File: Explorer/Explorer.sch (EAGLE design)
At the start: 42 parts, among them J4 POWER_JACK

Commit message: updated explorer board
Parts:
- removed D10, D11, D12, D13, D3, D4, D5, D6, D7, D8, D9: (no value), SparkFun-LED:LED0603
- removed D2: 1N4001, SparkFun-DiscreteSemi:DIODE-KIT2
- removed R2: 10k, SparkFun-Resistors:10KOHM-0603-1/10W-1%
- removed RESET: SKRKAEE020, D3ltav's Custom:SMD-BUTTON(2P-3.9X2.9X1.5+0.4MM)-SKRKAEE020
- added P10, P11, P12, P13, P2, P3, P4, P5, P6, P7, P8, P9: (no value), SparkFun-LED:LED0603
- added Q1, Q10, Q11, Q12, Q13, Q14, Q2, Q3, Q4, Q5, Q6, Q7, Q8, Q9: BSS138, SparkFun-DiscreteSemi:MOSFET-NCH-BSS138
- added R15, R16, R17, R18, R19, R20, R21, R22, R23, R24, R25, R26, R27, R28, R29, R30, R31, R32: 10k, SparkFun-Resistors:10KOHM-0603-1/10W-1%
- D1: value (none) -> 1N4001; device SparkFun-LED:LED0603 -> SparkFun-DiscreteSemi:DIODE-KIT2
- J2: device SparkFun-Connectors:CONN_19 -> SparkFun-Connectors:CONN_20
- ON: LCSC_PART (none) -> C49018
- R1: value 1k -> 10k; LCSC_PART (none) -> C25804
- R10, R11, R12, R13, R14, R3, R4, R5, R6, R7, R8, R9: LCSC_PART (none) -> C103556
- WIFI-BOOT, WIFI-RESET: LCSC_PART C465999 -> C455280
- renumbered J4 to J8, U1 to VR1
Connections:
- removed net N$8: R2.2, RESET.2
- new net L10: Q9.D, R23.2
- new net L11: Q10.D, R24.2
- new net L12: Q11.D, R25.2
- new net L13: Q12.D, R26.2
- new net L2: Q1.D, R15.2
- new net L3: Q2.D, R16.2
- new net L4: Q3.D, R17.2
- new net L5: Q4.D, R18.2
- new net L6: Q5.D, R19.2
- new net L7: Q6.D, R20.2
- new net L8: Q7.D, R21.2
- new net L9: Q8.D, R22.2
- new net MISO: B1.MISO, SPI.SDA
- new net MOSI: B1.MOSI, SPI.SCL
- new net N$10: P13.C, R26.1
- new net N$11: P12.C, R25.1
- new net N$12: P11.C, R24.1
- new net N$13: P10.C, R23.1
- new net N$14: P9.C, R22.1
- new net N$15: P8.C, R21.1
- new net N$16: P7.C, R20.1
- new net N$17: P6.C, R19.1
- new net N$18: P5.C, R18.1
- new net N$19: P4.C, R17.1
- new net N$20: P3.C, R16.1
- new net N$21: P2.C, R15.1
- new net SCK: B1.SCK, SPI.VCC
- new net SCL_3V: J1.SCL, Q13.S, R27.1
- new net SDA_3V: J1.SDA, Q14.S, R28.1
- net 3.3V: now also Q13.G, Q14.G, R27.2, R28.2
- net D10: now also Q9.G
- net D11: now also Q10.G
- net D12: now also Q11.G
- net D13: now also Q12.G
- net D2: now also Q1.G
- net D20_SDA: now also Q14.D, R30.1
- net D21_SCL: now also Q13.D, R29.1
- net D3: now also Q2.G
- net D4: now also Q3.G
- net D5: now also Q4.G
- net D6: now also Q5.G
- net D7: now also Q6.G
- net D8: now also Q7.G
- net D9: now also Q8.G
- net GND: now also Q1.S, Q10.S, Q11.S, Q12.S, Q2.S, Q3.S, Q4.S, Q5.S, Q6.S, Q7.S, Q8.S, Q9.S, R31.1, R32.1, SPI.GND; no longer R2.1
- net MEGARST: now also B1.!RESET!@2; no longer RESET.1
- net N$2: now also D1.A; no longer D2.A
- net N$4: now also R31.2, WIFI-RESET.2; no longer J1.SDA
- net N$9: now also R32.2, WIFI-BOOT.2; no longer J1.SCL
- net VCC: now also B1.VCC, P10.A, P11.A, P12.A, P13.A, P2.A, P3.A, P4.A, P5.A, P6.A, P7.A, P8.A, P9.A, R29.2, R30.2
- net VIN: now also B1.VIN, D1.C; no longer D2.C
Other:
- moved on the sheet: B1, J1, J3, R10, R11, R12, R13, R14, R3, R4, R5, R6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

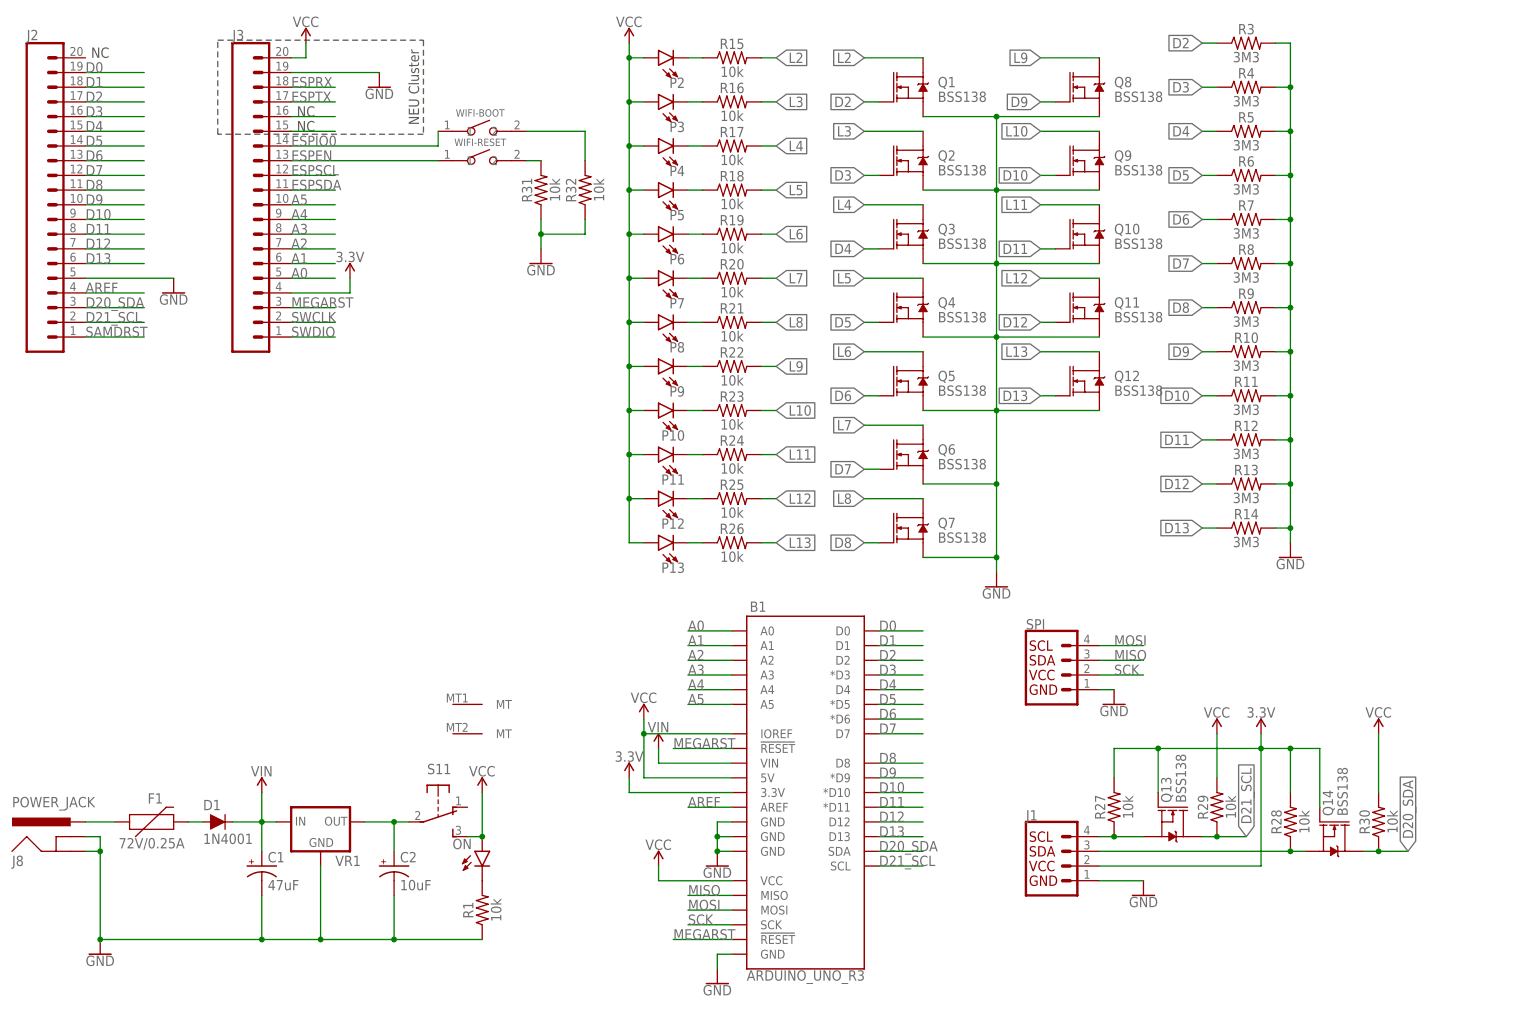
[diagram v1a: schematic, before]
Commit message: updated Explorer board to first prototype version
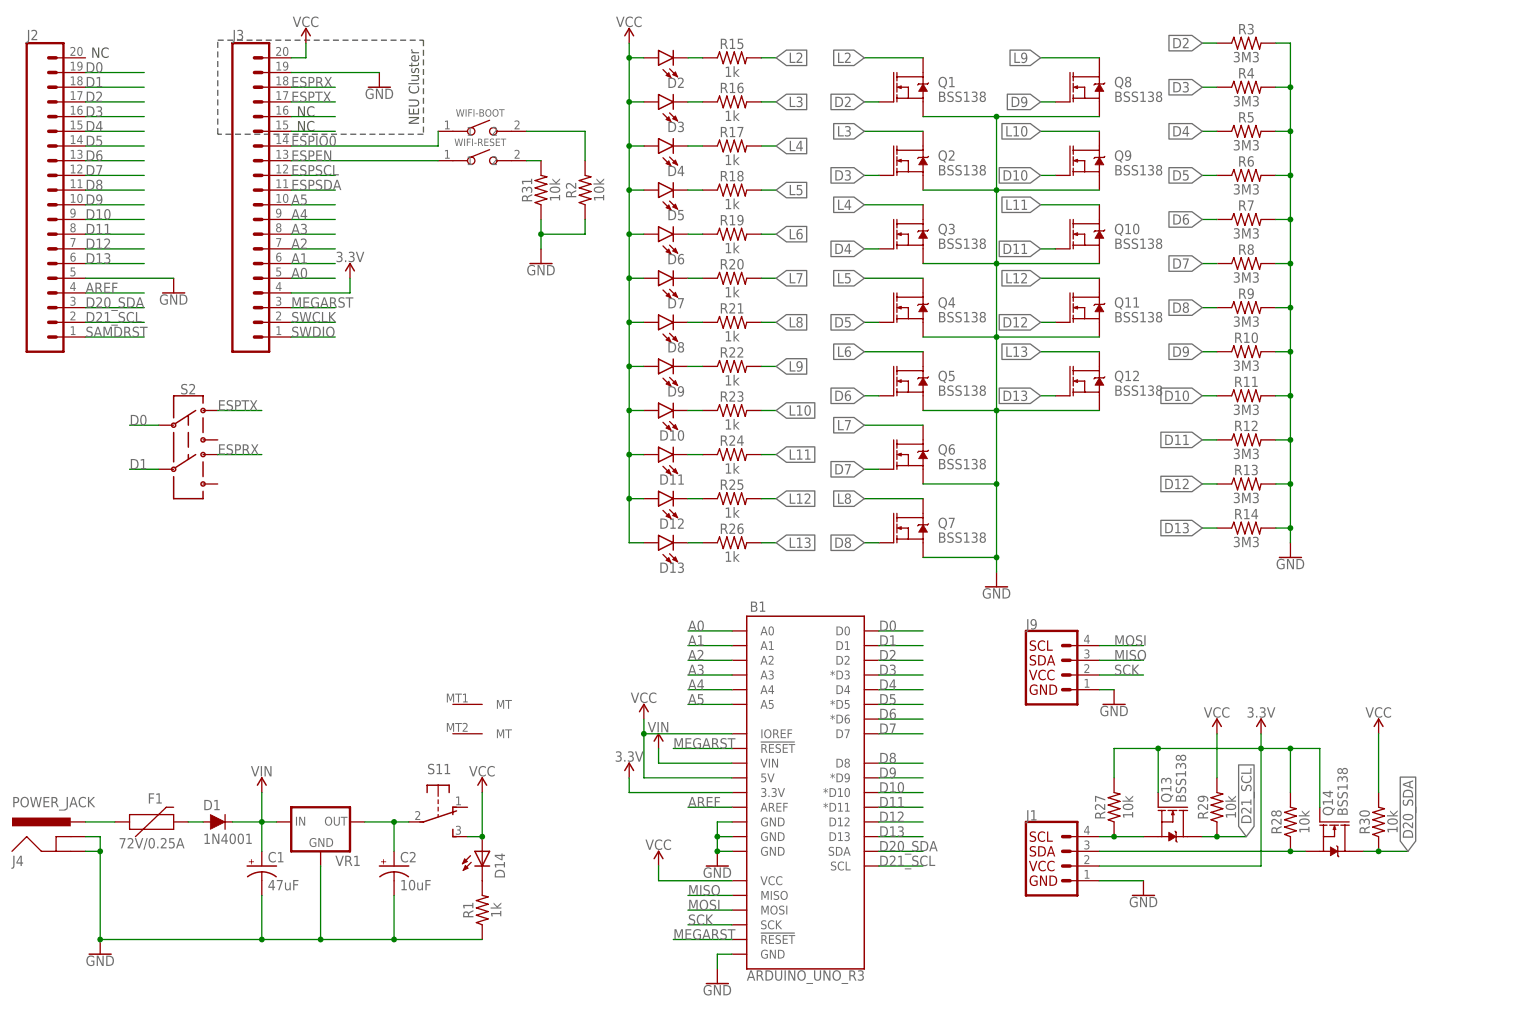
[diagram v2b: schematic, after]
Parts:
- removed ON: (no value), SparkFun-LED:LED1206
- added D14: (no value), adafruit:LEDCHIPLED_0805
- added S2: (no value), SparkFun-Switches:SWITCH-DPDT-SMD-AYZ0202
- J1: LCSC_PART (none) -> C239522; LCSC_PART_OLD (none) -> C145956
- J2, J3: LCSC_PART (none) -> C50984
- J9: LCSC_PART (none) -> C239522
- R1, R15, R16, R17, R18, R19, R20, R21, R22, R23, R24, R25, R26: value 10k -> 1k; LCSC_PART C25804 -> C21190
- renumbered J8 to J4, P10 to D10, P11 to D11, P12 to D12, P13 to D13, P2 to D2, P3 to D3, P4 to D4, P5 to D5, P6 to D6, P7 to D7, P8 to D8, P9 to D9, R32 to R2, SPI to J9
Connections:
- net D0: now also S2.2
- net D1: now also S2.5
- net ESPRX: now also S2.4
- net ESPTX: now also S2.1
- net N$6: now also D14.C; no longer ON.C
- net VCC: now also D14.A; no longer ON.A

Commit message: added gerber and necessary production files
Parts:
- removed R2, R31: 10k, SparkFun-Resistors:10KOHM-0603-1/10W-1%
- removed WIFI-RESET: SKRKAEE020, D3ltav's Custom:SMD-BUTTON(2P-3.9X2.9X1.5+0.4MM)-SKRKAEE020
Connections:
- removed net ESPEN: J3.13, WIFI-RESET.1
- removed net N$4: R31.2, WIFI-RESET.2
- removed net N$9: R2.2, WIFI-BOOT.2
- net GND: now also WIFI-BOOT.2; no longer R2.1, R31.1
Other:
- moved on the sheet: WIFI-BOOT
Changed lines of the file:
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@@
 </part>
 <part name="D1" library="SparkFun-DiscreteSemi" library_urn="urn:adsk.eagle:library:514" deviceset="DIODE" device="-KIT2" package3d_urn="urn:adsk.eagle:package:38455/1" value="1N4001"/>
-<part name="WIFI-RESET" library="D3ltav's Custom" deviceset="SMD-BUTTON(2P-3.9X2.9X1.5+0.4MM)" device="-SKRKAEE020" package3d_urn="urn:adsk.eagle:package:8005100/1" value="SKRKAEE020">
-<attribute name="LCSC_PART" value="C455280"/>
-</part>
 <part name="WIFI-BOOT" library="D3ltav's Custom" deviceset="SMD-BUTTON(2P-3.9X2.9X1.5+0.4MM)" device="-SKRKAEE020" package3d_urn="urn:adsk.eagle:package:8005100/1" value="SKRKAEE020">
 <attribute name="LCSC_PART" value="C455280"/>
@@
 <part name="SUPPLY11" library="SparkFun-PowerSymbols" library_urn="urn:adsk.eagle:library:530" deviceset="VCC" device=""/>
 <part name="SUPPLY12" library="SparkFun-PowerSymbols" library_urn="urn:adsk.eagle:library:530" deviceset="VIN" device=""/>
-<part name="R31" library="SparkFun-Resistors" library_urn="urn:adsk.eagle:library:532" deviceset="10KOHM" device="-0603-1/10W-1%" package3d_urn="urn:adsk.eagle:package:39650/1" value="10k">
-<attribute name="LCSC_PART" value="C25804"/>
-</part>
-<part name="R2" library="SparkFun-Resistors" library_urn="urn:adsk.eagle:library:532" deviceset="10KOHM" device="-0603-1/10W-1%" package3d_urn="urn:adsk.eagle:package:39650/1" value="10k">
-<attribute name="LCSC_PART" value="C25804"/>
-</part>
 <part name="GND11" library="SparkFun-PowerSymbols" library_urn="urn:adsk.eagle:library:530" deviceset="GND" device=""/>
 <part name="S2" library="SparkFun-Switches" library_urn="urn:adsk.eagle:library:535" deviceset="SWITCH-DPDT" device="-SMD-AYZ0202" package3d_urn="urn:adsk.eagle:package:40160/1">
@@
 <attribute name="VALUE" x="38.1" y="36.068" size="1.778" layer="96" font="vector" align="top-left"/>
 </instance>
-<instance part="WIFI-RESET" gate="G$1" x="86.36" y="152.4" smashed="yes">
-<attribute name="NAME" x="81.534" y="154.94" size="1.27" layer="95" ratio="10"/>
-</instance>
-<instance part="WIFI-BOOT" gate="G$1" x="86.36" y="157.48" smashed="yes">
-<attribute name="NAME" x="81.788" y="160.02" size="1.27" layer="95" ratio="10"/>
+<instance part="WIFI-BOOT" gate="G$1" x="86.36" y="154.94" smashed="yes">
+<attribute name="NAME" x="81.788" y="157.48" size="1.27" layer="95" ratio="10"/>
 </instance>
 <instance part="R1" gate="G$1" x="86.36" y="22.86" smashed="yes" rot="R90">
@@
 <instance part="SUPPLY12" gate="G$1" x="116.84" y="50.8" smashed="yes">
 <attribute name="VALUE" x="116.84" y="53.594" size="1.778" layer="96" align="bottom-center"/>
-</instance>
-<instance part="R31" gate="G$1" x="96.52" y="147.32" smashed="yes" rot="R90">
-<attribute name="NAME" x="94.996" y="147.32" size="1.778" layer="95" font="vector" rot="R90" align="bottom-center"/>
-<attribute name="VALUE" x="98.044" y="147.32" size="1.778" layer="96" font="vector" rot="R90" align="top-center"/>
-<attribute name="LCSC_PART" x="96.52" y="147.32" size="1.778" layer="96" rot="R90" display="off"/>
-</instance>
-<instance part="R2" gate="G$1" x="104.14" y="147.32" smashed="yes" rot="R90">
-<attribute name="NAME" x="102.616" y="147.32" size="1.778" layer="95" font="vector" rot="R90" align="bottom-center"/>
-<attribute name="VALUE" x="105.664" y="147.32" size="1.778" layer="96" font="vector" rot="R90" align="top-center"/>
-<attribute name="LCSC_PART" x="104.14" y="147.32" size="1.778" layer="96" rot="R90" display="off"/>
 </instance>
 <instance part="GND11" gate="1" x="96.52" y="134.62" smashed="yes">
@@
 <segment>
 <pinref part="GND11" gate="1" pin="GND"/>
-<pinref part="R31" gate="G$1" pin="1"/>
-<wire x1="96.52" y1="137.16" x2="96.52" y2="139.7" width="0.1524" layer="91"/>
-<pinref part="R2" gate="G$1" pin="1"/>
-<wire x1="96.52" y1="139.7" x2="96.52" y2="142.24" width="0.1524" layer="91"/>
-<wire x1="104.14" y1="142.24" x2="104.14" y2="139.7" width="0.1524" layer="91"/>
-<wire x1="104.14" y1="139.7" x2="96.52" y2="139.7" width="0.1524" layer="91"/>
-<junction x="96.52" y="139.7"/>
+<wire x1="96.52" y1="137.16" x2="96.52" y2="154.94" width="0.1524" layer="91"/>
+<pinref part="WIFI-BOOT" gate="G$1" pin="2"/>
+<wire x1="96.52" y1="154.94" x2="93.98" y2="154.94" width="0.1524" layer="91"/>
 </segment>
 </net>
@@
 <label x="53.34" y="154.94" size="1.778" layer="95"/>
 <pinref part="WIFI-BOOT" gate="G$1" pin="1"/>
-<wire x1="78.74" y1="157.48" x2="78.74" y2="154.94" width="0.1524" layer="91"/>
 <wire x1="78.74" y1="154.94" x2="53.34" y2="154.94" width="0.1524" layer="91"/>
-</segment>
-</net>
-<net name="ESPEN" class="0">
-<segment>
-<pinref part="J3" gate="G$1" pin="13"/>
-<label x="53.34" y="152.4" size="1.778" layer="95"/>
-<pinref part="WIFI-RESET" gate="G$1" pin="1"/>
-<wire x1="78.74" y1="152.4" x2="53.34" y2="152.4" width="0.1524" layer="91"/>
 </segment>
 </net>
@@
 </segment>
 </net>
-<net name="N$4" class="0">
-<segment>
-<pinref part="WIFI-RESET" gate="G$1" pin="2"/>
-<pinref part="R31" gate="G$1" pin="2"/>
-<wire x1="93.98" y1="152.4" x2="96.52" y2="152.4" width="0.1524" layer="91"/>
-</segment>
-</net>
-<net name="N$9" class="0">
-<segment>
-<pinref part="WIFI-BOOT" gate="G$1" pin="2"/>
-<wire x1="93.98" y1="157.48" x2="104.14" y2="157.48" width="0.1524" layer="91"/>
-<pinref part="R2" gate="G$1" pin="2"/>
-<wire x1="104.14" y1="157.48" x2="104.14" y2="152.4" width="0.1524" layer="91"/>
-</segment>
-</net>
